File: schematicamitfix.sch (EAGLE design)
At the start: 35 parts, among them J1 FTDI_DEVICE, M1 WIRELESS-NRF24L01, U1 ATMEGA328P_TQFP, U2 GY-521MPU6050

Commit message: Updated PWM pins
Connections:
- removed net N$12: U$12.G, U1.PC2(ADC2)
- removed net N$16: R5.2, U$16.G, U1.PC3(ADC3)
- removed net N$3: R3.2, U$5.G, U1.PC1(ADC1)
- removed net N$8: R2.2, U$8.G, U1.PC0(ADC0)
- new net PWM1: R2.2, U$8.G
- new net PWM2: R3.2, U$5.G
- new net PWM3: R4.2, U$12.G
- new net PWM4: R5.2, U$16.G
- net 0: now also R4.1
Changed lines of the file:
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@@
 </segment>
 </net>
-<net name="N$3" class="0">
+<net name="PWM2" class="0">
 <segment>
 <wire x1="210.82" y1="60.96" x2="236.22" y2="60.96" width="0.1524" layer="91"/>
 <wire x1="236.22" y1="60.96" x2="236.22" y2="38.1" width="0.1524" layer="91"/>
 <pinref part="U$5" gate="G$1" pin="G"/>
-<pinref part="U1" gate="U$1" pin="PC1(ADC1)"/>
 <wire x1="236.22" y1="38.1" x2="236.22" y2="22.86" width="0.1524" layer="91"/>
-<wire x1="86.36" y1="66.04" x2="210.82" y2="66.04" width="0.1524" layer="91"/>
-<wire x1="210.82" y1="66.04" x2="210.82" y2="60.96" width="0.1524" layer="91"/>
 <pinref part="R3" gate="G$1" pin="2"/>
 <wire x1="236.22" y1="38.1" x2="220.98" y2="38.1" width="0.1524" layer="91"/>
 <wire x1="220.98" y1="38.1" x2="220.98" y2="40.64" width="0.1524" layer="91"/>
 <junction x="236.22" y="38.1"/>
+<label x="210.82" y="60.96" size="1.778" layer="95" rot="R180" xref="yes"/>
 </segment>
 </net>
@@
 </segment>
 </net>
-<net name="N$8" class="0">
-<segment>
-<wire x1="246.38" y1="198.12" x2="269.24" y2="198.12" width="0.1524" layer="91"/>
-<wire x1="269.24" y1="198.12" x2="271.78" y2="198.12" width="0.1524" layer="91"/>
-<wire x1="271.78" y1="198.12" x2="271.78" y2="180.34" width="0.1524" layer="91"/>
-<pinref part="U$8" gate="G$1" pin="G"/>
-<pinref part="U1" gate="U$1" pin="PC0(ADC0)"/>
-<wire x1="271.78" y1="180.34" x2="271.78" y2="160.02" width="0.1524" layer="91"/>
-<wire x1="86.36" y1="68.58" x2="152.4" y2="68.58" width="0.1524" layer="91"/>
-<wire x1="152.4" y1="68.58" x2="152.4" y2="200.66" width="0.1524" layer="91"/>
-<wire x1="152.4" y1="200.66" x2="269.24" y2="200.66" width="0.1524" layer="91"/>
-<wire x1="269.24" y1="200.66" x2="269.24" y2="198.12" width="0.1524" layer="91"/>
-<junction x="269.24" y="198.12"/>
-<pinref part="R2" gate="G$1" pin="2"/>
-<wire x1="271.78" y1="180.34" x2="251.46" y2="180.34" width="0.1524" layer="91"/>
-<junction x="271.78" y="180.34"/>
-</segment>
-</net>
 <net name="N$9" class="0">
 <segment>
@@
 </segment>
 </net>
-<net name="N$12" class="0">
+<net name="PWM3" class="0">
 <segment>
 <wire x1="332.74" y1="-99.06" x2="358.14" y2="-99.06" width="0.1524" layer="91"/>
-<wire x1="358.14" y1="-99.06" x2="358.14" y2="-137.16" width="0.1524" layer="91"/>
+<wire x1="358.14" y1="-99.06" x2="358.14" y2="-127" width="0.1524" layer="91"/>
 <pinref part="U$12" gate="G$1" pin="G"/>
-<pinref part="U1" gate="U$1" pin="PC2(ADC2)"/>
-<wire x1="86.36" y1="63.5" x2="157.48" y2="63.5" width="0.1524" layer="91"/>
-<wire x1="157.48" y1="63.5" x2="157.48" y2="-119.38" width="0.1524" layer="91"/>
-<wire x1="157.48" y1="-119.38" x2="332.74" y2="-119.38" width="0.1524" layer="91"/>
-<wire x1="332.74" y1="-119.38" x2="332.74" y2="-99.06" width="0.1524" layer="91"/>
+<label x="332.74" y="-99.06" size="1.778" layer="95" rot="R180" xref="yes"/>
+<pinref part="R4" gate="G$1" pin="2"/>
+<wire x1="358.14" y1="-127" x2="358.14" y2="-137.16" width="0.1524" layer="91"/>
+<wire x1="322.58" y1="-127" x2="358.14" y2="-127" width="0.1524" layer="91"/>
+<junction x="358.14" y="-127"/>
 </segment>
 </net>
@@
 </segment>
 </net>
-<net name="N$16" class="0">
+<net name="PWM4" class="0">
 <segment>
 <wire x1="210.82" y1="-220.98" x2="236.22" y2="-220.98" width="0.1524" layer="91"/>
 <wire x1="236.22" y1="-220.98" x2="236.22" y2="-259.08" width="0.1524" layer="91"/>
 <pinref part="U$16" gate="G$1" pin="G"/>
-<pinref part="U1" gate="U$1" pin="PC3(ADC3)"/>
-<wire x1="86.36" y1="60.96" x2="127" y2="60.96" width="0.1524" layer="91"/>
-<wire x1="127" y1="60.96" x2="127" y2="-238.76" width="0.1524" layer="91"/>
 <wire x1="127" y1="-238.76" x2="185.42" y2="-238.76" width="0.1524" layer="91"/>
 <wire x1="185.42" y1="-238.76" x2="210.82" y2="-238.76" width="0.1524" layer="91"/>
@@
 <wire x1="185.42" y1="-238.76" x2="185.42" y2="-248.92" width="0.1524" layer="91"/>
 <junction x="185.42" y="-238.76"/>
+<label x="127" y="-238.76" size="1.778" layer="95" rot="R180" xref="yes"/>
 </segment>
 </net>
@@
 <wire x1="111.76" y1="10.16" x2="111.76" y2="5.08" width="0.1524" layer="91"/>
 </segment>
+<segment>
+<pinref part="R4" gate="G$1" pin="1"/>
+<pinref part="X_6" gate="G$1" pin="0"/>
+<wire x1="322.58" y1="-137.16" x2="322.58" y2="-144.78" width="0.1524" layer="91"/>
+</segment>
 </net>
 <net name="N$7" class="0">
@@
 </segment>
 </net>
+<net name="PWM1" class="0">
+<segment>
+<pinref part="R2" gate="G$1" pin="2"/>
+<pinref part="U$8" gate="G$1" pin="G"/>
+<wire x1="246.38" y1="198.12" x2="271.78" y2="198.12" width="0.1524" layer="91"/>
+<wire x1="271.78" y1="198.12" x2="271.78" y2="180.34" width="0.1524" layer="91"/>
+<wire x1="271.78" y1="180.34" x2="271.78" y2="160.02" width="0.1524" layer="91"/>
+<junction x="271.78" y="180.34"/>
+<wire x1="271.78" y1="180.34" x2="251.46" y2="180.34" width="0.1524" layer="91"/>
+<label x="246.38" y="198.12" size="1.778" layer="95" rot="R180" xref="yes"/>
+</segment>
+</net>

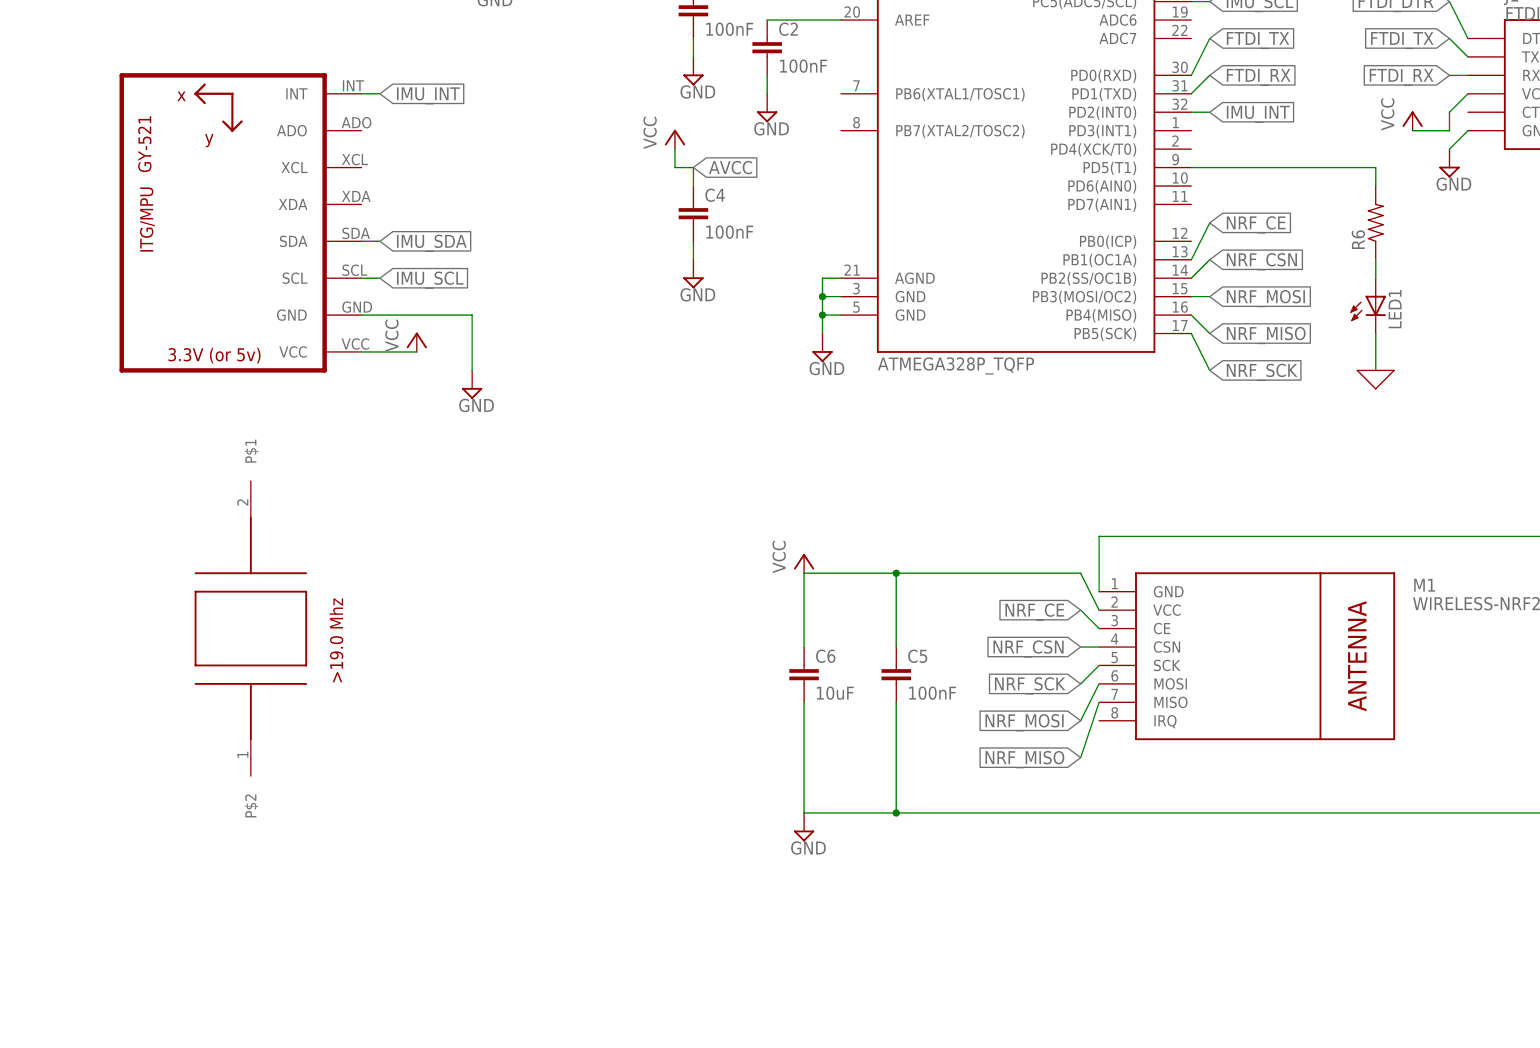
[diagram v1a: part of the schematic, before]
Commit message: Added circuit for crystal oscillator
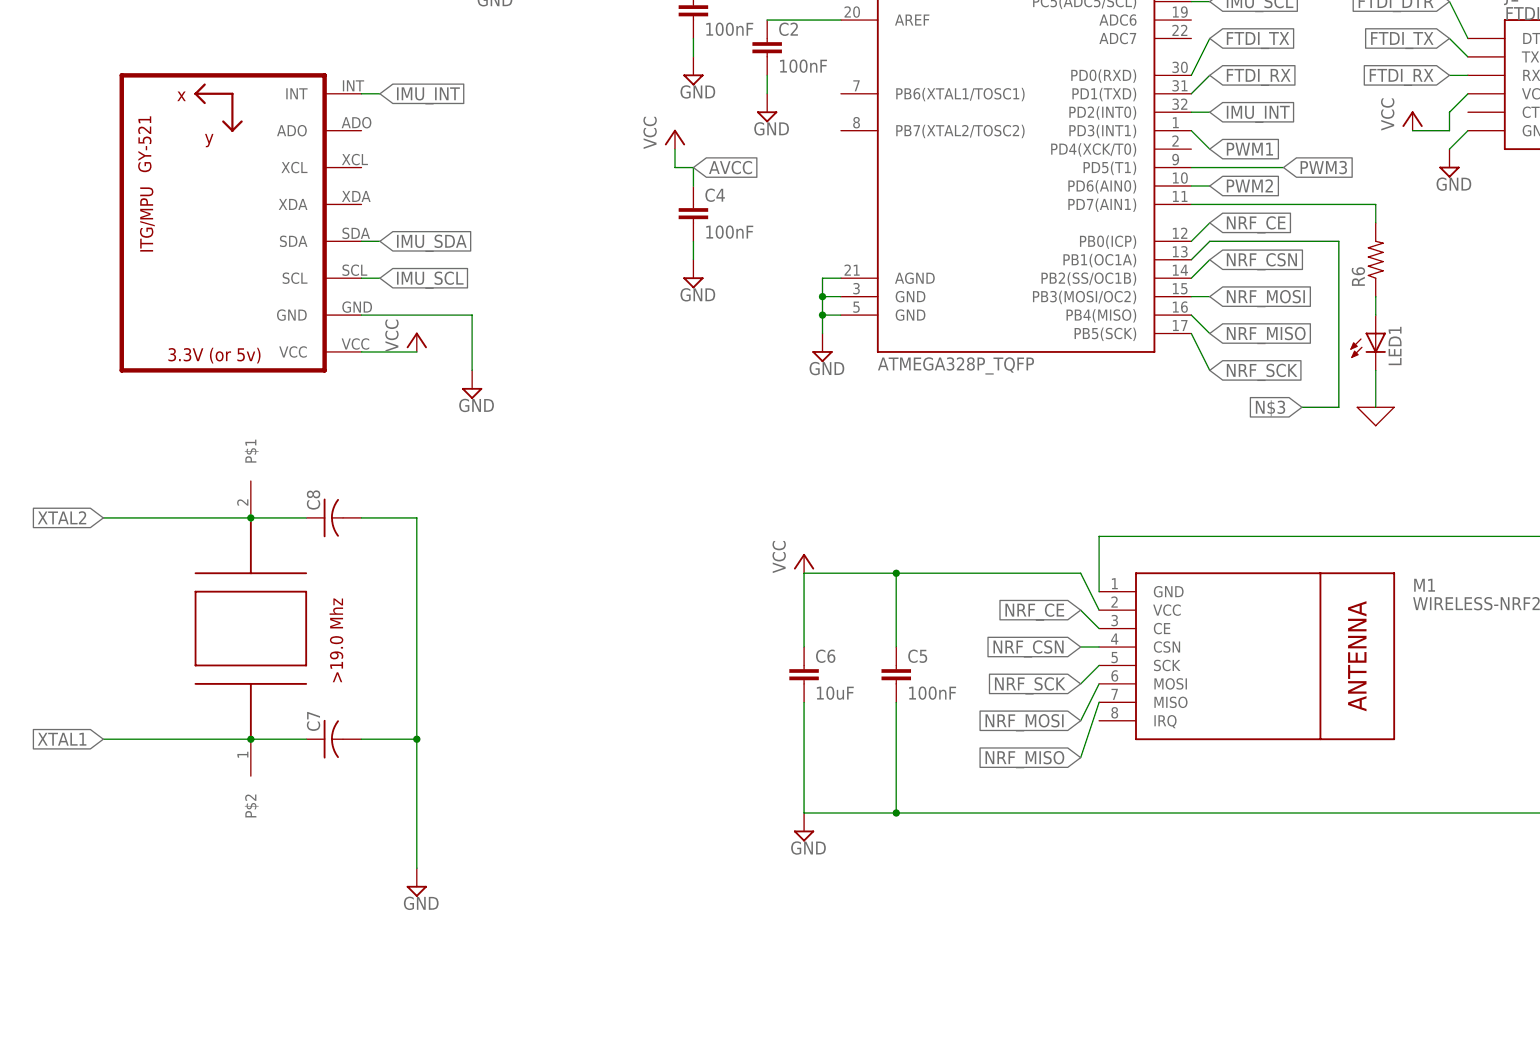
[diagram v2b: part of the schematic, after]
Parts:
- added C7, C8: (no value), rcl:C-USC0603
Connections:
- new net N$3: U1.PB1(OC1A)
- new net N$8: C7.2, C8.2
- new net XTAL1: C7.1, U$17.P$2
- new net XTAL2: C8.1, U$17.P$1
- net N$7: now also U1.PD7(AIN1); no longer U1.PD5(T1)
- net NRF_CE: now also U1.PB0(ICP); no longer U1.PB1(OC1A)
- net PWM1: now also U1.PD3(INT1)
- net PWM2: now also U1.PD6(AIN0)
- net PWM3: now also U1.PD5(T1)
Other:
- moved on the sheet: LED1, R6
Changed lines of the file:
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@@
 <part name="X_9" library="ngspice-simulation" library_urn="urn:adsk.eagle:library:527439" deviceset="GND" device=""/>
 <part name="U$17" library="LFXTAL019715" deviceset="LFXTAL019715" device=""/>
+<part name="C7" library="rcl" library_urn="urn:adsk.eagle:library:334" deviceset="C-US" device="C0603" package3d_urn="urn:adsk.eagle:package:23616/2"/>
+<part name="C8" library="rcl" library_urn="urn:adsk.eagle:library:334" deviceset="C-US" device="C0603" package3d_urn="urn:adsk.eagle:package:23616/2"/>
+<part name="SUPPLY9" library="supply2" library_urn="urn:adsk.eagle:library:372" deviceset="GND" device=""/>
 </parts>
 <sheets>
@@
 <instance part="X_7" gate="G$1" x="200.66" y="40.64" rot="R270"/>
 <instance part="X_8" gate="G$1" x="236.22" y="180.34" rot="R270"/>
-<instance part="LED1" gate="G$1" x="111.76" y="15.24"/>
-<instance part="R6" gate="G$1" x="111.76" y="25.4" rot="R90"/>
-<instance part="X_9" gate="G$1" x="111.76" y="5.08"/>
+<instance part="LED1" gate="G$1" x="111.76" y="10.16"/>
+<instance part="R6" gate="G$1" x="111.76" y="20.32" rot="R90"/>
+<instance part="X_9" gate="G$1" x="111.76" y="0"/>
 <instance part="U$17" gate="G$1" x="-43.18" y="-30.48" rot="R90"/>
+<instance part="C7" gate="G$1" x="-33.02" y="-45.72" rot="R90"/>
+<instance part="C8" gate="G$1" x="-33.02" y="-15.24" rot="R90"/>
+<instance part="SUPPLY9" gate="GND" x="-20.32" y="-66.04"/>
 </instances>
 <busses>
@@
 </segment>
 <segment>
-<pinref part="U1" gate="U$1" pin="PB1(OC1A)"/>
-<wire x1="86.36" y1="20.32" x2="88.9" y2="25.4" width="0.1524" layer="91"/>
+<pinref part="U1" gate="U$1" pin="PB0(ICP)"/>
+<wire x1="86.36" y1="22.86" x2="88.9" y2="25.4" width="0.1524" layer="91"/>
 <label x="88.9" y="25.4" size="1.778" layer="95" xref="yes"/>
 </segment>
@@
 <label x="210.82" y="60.96" size="1.778" layer="95" rot="R180" xref="yes"/>
 </segment>
+<segment>
+<pinref part="U1" gate="U$1" pin="PD6(AIN0)"/>
+<wire x1="86.36" y1="30.48" x2="88.9" y2="30.48" width="0.1524" layer="91"/>
+<label x="88.9" y="30.48" size="1.778" layer="95" xref="yes"/>
+</segment>
 </net>
 <net name="N$5" class="0">
@@
 <wire x1="322.58" y1="-127" x2="358.14" y2="-127" width="0.1524" layer="91"/>
 <junction x="358.14" y="-127"/>
+</segment>
+<segment>
+<pinref part="U1" gate="U$1" pin="PD5(T1)"/>
+<wire x1="86.36" y1="33.02" x2="99.06" y2="33.02" width="0.1524" layer="91"/>
+<label x="99.06" y="33.02" size="1.778" layer="95" xref="yes"/>
 </segment>
 </net>
@@
 <pinref part="LED1" gate="G$1" pin="C"/>
 <pinref part="X_9" gate="G$1" pin="0"/>
-<wire x1="111.76" y1="10.16" x2="111.76" y2="5.08" width="0.1524" layer="91"/>
+<wire x1="111.76" y1="5.08" x2="111.76" y2="0" width="0.1524" layer="91"/>
 </segment>
 <segment>
@@
 <net name="N$7" class="0">
 <segment>
-<pinref part="U1" gate="U$1" pin="PD5(T1)"/>
-<wire x1="86.36" y1="33.02" x2="111.76" y2="33.02" width="0.1524" layer="91"/>
 <pinref part="R6" gate="G$1" pin="2"/>
-<wire x1="111.76" y1="33.02" x2="111.76" y2="30.48" width="0.1524" layer="91"/>
+<wire x1="111.76" y1="27.94" x2="111.76" y2="25.4" width="0.1524" layer="91"/>
+<pinref part="U1" gate="U$1" pin="PD7(AIN1)"/>
+<wire x1="111.76" y1="27.94" x2="86.36" y2="27.94" width="0.1524" layer="91"/>
 </segment>
 </net>
@@
 <pinref part="R6" gate="G$1" pin="1"/>
 <pinref part="LED1" gate="G$1" pin="A"/>
-<wire x1="111.76" y1="20.32" x2="111.76" y2="17.78" width="0.1524" layer="91"/>
+<wire x1="111.76" y1="15.24" x2="111.76" y2="12.7" width="0.1524" layer="91"/>
 </segment>
 </net>
@@
 <label x="246.38" y="198.12" size="1.778" layer="95" rot="R180" xref="yes"/>
 </segment>
-</net>
+<segment>
+<pinref part="U1" gate="U$1" pin="PD3(INT1)"/>
+<wire x1="86.36" y1="38.1" x2="88.9" y2="35.56" width="0.1524" layer="91"/>
+<label x="88.9" y="35.56" size="1.778" layer="95" xref="yes"/>
+</segment>
+</net>
+<net name="N$3" class="0">
+<segment>
+<pinref part="U1" gate="U$1" pin="PB1(OC1A)"/>
+<wire x1="86.36" y1="20.32" x2="88.9" y2="22.86" width="0.1524" layer="91"/>
+<wire x1="88.9" y1="22.86" x2="106.68" y2="22.86" width="0.1524" layer="91"/>
+<wire x1="106.68" y1="22.86" x2="106.68" y2="0" width="0.1524" layer="91"/>
+<wire x1="106.68" y1="0" x2="101.6" y2="0" width="0.1524" layer="91"/>
+<label x="101.6" y="0" size="1.778" layer="95" rot="R180" xref="yes"/>
+</segment>
+</net>
+<net name="XTAL2" class="0">
+<segment>
+<pinref part="U$17" gate="G$1" pin="P$1"/>
+<wire x1="-63.5" y1="-15.24" x2="-43.18" y2="-15.24" width="0.1524" layer="91"/>
+<junction x="-43.18" y="-15.24"/>
+<wire x1="-43.18" y1="-15.24" x2="-35.56" y2="-15.24" width="0.1524" layer="91"/>
+<pinref part="C8" gate="G$1" pin="1"/>
+<label x="-63.5" y="-15.24" size="1.778" layer="95" rot="R180" xref="yes"/>
+</segment>
+</net>
+<net name="N$8" class="0">
+<segment>
+<pinref part="C7" gate="G$1" pin="2"/>
+<wire x1="-20.32" y1="-45.72" x2="-27.94" y2="-45.72" width="0.1524" layer="91"/>
+<wire x1="-20.32" y1="-45.72" x2="-20.32" y2="-63.5" width="0.1524" layer="91"/>
+<junction x="-20.32" y="-45.72"/>
+<pinref part="C8" gate="G$1" pin="2"/>
+<wire x1="-27.94" y1="-15.24" x2="-20.32" y2="-15.24" width="0.1524" layer="91"/>
+<wire x1="-20.32" y1="-15.24" x2="-20.32" y2="-45.72" width="0.1524" layer="91"/>
+</segment>
+</net>
+<net name="XTAL1" class="0">
+<segment>
+<pinref part="U$17" gate="G$1" pin="P$2"/>
+<wire x1="-43.18" y1="-45.72" x2="-35.56" y2="-45.72" width="0.1524" layer="91"/>
+<pinref part="C7" gate="G$1" pin="1"/>
+<wire x1="-43.18" y1="-45.72" x2="-63.5" y2="-45.72" width="0.1524" layer="91"/>
+<junction x="-43.18" y="-45.72"/>
+<label x="-63.5" y="-45.72" size="1.778" layer="95" rot="R180" xref="yes"/>
+</segment>
+</net>

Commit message: Fixed stuff. Replaced crystal & voltage regulator.
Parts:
- removed U$13, U$2, U$9: JST_CONNECTOR_FEMALE, quad:JST_CONNECTOR_FEMALE
- removed U$17: (no value), LFXTAL019715:LFXTAL019715
- added C10: 0.47uF, rcl:C-EUC0603
- added C11, C9: 2.2uF, rcl:C-EUC0603
- added C13: 100uF, rcl:C-EUC1210
- added R8, R9: 10k, rcl:R-US_R0603
- added U$19: JST_CONNECTOR_FEMALE, quad:JST_CONNECTOR_FEMALE
- added U3: MAX1595EUA33+, MAX1595EUA33+:MAX1595EUA33+
- C7, C8: value (none) -> 22pF
- R6: value (none) -> 100 ohms
- U$1: value JST_CONNECTOR_FEMALE -> ABLS-8.000MHZ-B4-T; device quad:JST_CONNECTOR_FEMALE -> ABLS-8.000MHZ-B4-T:ABLS-8.000MHZ-B4-T
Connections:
- removed net 0: LED1.C, R2.1, R3.1, R4.1, R5.1, U$1.-, U$12.S, U$13.-, U$16.S, U$2.-, U$5.S, U$8.S, U$9.-
- removed net N$14: U$10.GPIN, U$11.+, U$9.+
- new net AIN: R8.1, R9.2, U1.PC0(ADC0)
- new net N$15: U3.GND, U3.PGND
- new net N$16: R9.1
- new net N$19: U3.AOUT, U3.OUT
- new net N$20: C13.1, U$19.-
- new net N$22: R5.1
- new net N$28: U$16.S
- new net N$29: R3.1
- new net N$30: U$5.S
- new net N$31: R2.1
- new net N$32: U$8.S
- new net N$33: LED1.C
- new net VIN: C13.2, R8.2, U$10.GPIN, U$11.+, U$14.GPIN, U$15.+, U$19.+, U$3.+, U$4.GPIN, U$6.GPIN, U$7.+, U3.!SHDN, U3.IN
- net N$10: now also U3.CXN; no longer U$2.+, U$6.GPIN, U$7.+
- net N$18: now also U$12.S; no longer U$13.+, U$14.GPIN, U$15.+
- net N$3: now also R4.1; no longer U1.PB1(OC1A)
- net N$6: now also U3.CXP; no longer U$1.+, U$3.+, U$4.GPIN
- net PWM4: now also U1.PB1(OC1A)
- net XTAL1: now also U$1.1, U1.PB6(XTAL1/TOSC1); no longer U$17.P$2
- net XTAL2: now also U$1.2, U1.PB7(XTAL2/TOSC2); no longer U$17.P$1

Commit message: Fixed RX and TX connections
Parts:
- C11: value 2.2uF -> 100nF
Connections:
- net FTDI_RX: now also U1.PD0(RXD); no longer U1.PD1(TXD)
- net FTDI_TX: now also U1.PD1(TXD); no longer U1.PD0(RXD)
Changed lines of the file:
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@@
 <part name="C9" library="rcl" library_urn="urn:adsk.eagle:library:334" deviceset="C-EU" device="C0603" package3d_urn="urn:adsk.eagle:package:23616/2" value="2.2uF"/>
 <part name="C10" library="rcl" library_urn="urn:adsk.eagle:library:334" deviceset="C-EU" device="C0603" package3d_urn="urn:adsk.eagle:package:23616/2" value="0.47uF"/>
-<part name="C11" library="rcl" library_urn="urn:adsk.eagle:library:334" deviceset="C-EU" device="C0603" package3d_urn="urn:adsk.eagle:package:23616/2" value="2.2uF"/>
+<part name="C11" library="rcl" library_urn="urn:adsk.eagle:library:334" deviceset="C-EU" device="C0603" package3d_urn="urn:adsk.eagle:package:23616/2" value="100nF"/>
 </parts>
 <sheets>
@@
 </segment>
 <segment>
+<pinref part="U1" gate="U$1" pin="PD1(TXD)"/>
+<wire x1="86.36" y1="43.18" x2="88.9" y2="45.72" width="0.1524" layer="91"/>
+<label x="88.9" y="45.72" size="1.778" layer="95" xref="yes"/>
+</segment>
+</net>
+<net name="FTDI_RX" class="0">
+<segment>
+<pinref part="J1" gate="G$1" pin="RXI"/>
+<wire x1="124.46" y1="45.72" x2="121.92" y2="45.72" width="0.1524" layer="91"/>
+<label x="121.92" y="45.72" size="1.778" layer="95" rot="R180" xref="yes"/>
+</segment>
+<segment>
 <pinref part="U1" gate="U$1" pin="PD0(RXD)"/>
 <wire x1="86.36" y1="45.72" x2="88.9" y2="50.8" width="0.1524" layer="91"/>
@@
 </segment>
 </net>
-<net name="FTDI_RX" class="0">
-<segment>
-<pinref part="J1" gate="G$1" pin="RXI"/>
-<wire x1="124.46" y1="45.72" x2="121.92" y2="45.72" width="0.1524" layer="91"/>
-<label x="121.92" y="45.72" size="1.778" layer="95" rot="R180" xref="yes"/>
-</segment>
-<segment>
-<pinref part="U1" gate="U$1" pin="PD1(TXD)"/>
-<wire x1="86.36" y1="43.18" x2="88.9" y2="45.72" width="0.1524" layer="91"/>
-<label x="88.9" y="45.72" size="1.778" layer="95" xref="yes"/>
-</segment>
-</net>
